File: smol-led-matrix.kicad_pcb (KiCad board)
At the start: 4 copper layers, 45.8 x 20.4 mm, 323 parts, among them J1 USB_C_Receptacle_USB2.0, J2 TagConnect_TC2030_SWD, Q1 FS8205, Q2 AO3401A, SW1 SW_Push, SW2 SW_Push, U1 STM32L433CBTx, U2 TP4054, U3 DW01+G, U4 XC6206P332MR

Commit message: Finish routing on first unit
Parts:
- added REF**: Perforation_0.2mm, Perforation:Perforation_0.2mm, F.Cu at (108.0, 142.7)
- added REF**: Perforation_0.2mm, Perforation:Perforation_0.2mm, F.Cu at (62.0, 131.8)
- added REF**: Perforation_0.2mm, Perforation:Perforation_0.2mm, F.Cu at (62.0, 129.8)
- added REF**: Perforation_0.2mm, Perforation:Perforation_0.2mm, F.Cu at (62.0, 138.7)
- added REF**: Perforation_0.2mm, Perforation:Perforation_0.2mm, F.Cu at (62.0, 140.7)
- added REF**: Perforation_0.2mm, Perforation:Perforation_0.2mm, F.Cu at (62.0, 142.7)
- added REF**: Perforation_0.2mm, Perforation:Perforation_0.2mm, F.Cu at (62.0, 139.7)
- added REF**: Perforation_0.2mm, Perforation:Perforation_0.2mm, F.Cu at (62.0, 141.2)
- added REF**: Perforation_0.2mm, Perforation:Perforation_0.2mm, F.Cu at (62.0, 139.2)
- added REF**: Perforation_0.2mm, Perforation:Perforation_0.2mm, F.Cu at (62.0, 141.7)
- added REF**: Perforation_0.2mm, Perforation:Perforation_0.2mm, F.Cu at (62.0, 138.2)
- added REF**: Perforation_0.2mm, Perforation:Perforation_0.2mm, F.Cu at (62.0, 128.3)
- added REF**: Perforation_0.2mm, Perforation:Perforation_0.2mm, F.Cu at (62.0, 142.2)
- added REF**: Perforation_0.2mm, Perforation:Perforation_0.2mm, F.Cu at (62.0, 140.2)
- added REF**: Perforation_0.2mm, Perforation:Perforation_0.2mm, F.Cu at (108.0, 139.3)
- added REF**: Perforation_0.2mm, Perforation:Perforation_0.2mm, F.Cu at (108.0, 141.2)
- added REF**: Perforation_0.2mm, Perforation:Perforation_0.2mm, F.Cu at (108.0, 142.2)
- added REF**: Perforation_0.2mm, Perforation:Perforation_0.2mm, F.Cu at (108.0, 140.8)
- added REF**: Perforation_0.2mm, Perforation:Perforation_0.2mm, F.Cu at (108.0, 140.2)
- added REF**: Perforation_0.2mm, Perforation:Perforation_0.2mm, F.Cu at (108.0, 139.8)
- added REF**: Perforation_0.2mm, Perforation:Perforation_0.2mm, F.Cu at (108.0, 138.8)
- added REF**: Perforation_0.2mm, Perforation:Perforation_0.2mm, F.Cu at (108.0, 138.2)
- added REF**: Perforation_0.2mm, Perforation:Perforation_0.2mm, F.Cu at (62.0, 130.3)
- added REF**: Perforation_0.2mm, Perforation:Perforation_0.2mm, F.Cu at (108.0, 141.8)
- added REF**: Perforation_0.2mm, Perforation:Perforation_0.2mm, F.Cu at (108.0, 132.3)
- added REF**: Perforation_0.2mm, Perforation:Perforation_0.2mm, F.Cu at (108.0, 130.3)
- added REF**: Perforation_0.2mm, Perforation:Perforation_0.2mm, F.Cu at (108.0, 128.8)
- added REF**: Perforation_0.2mm, Perforation:Perforation_0.2mm, F.Cu at (108.0, 127.8)
- added REF**: Perforation_0.2mm, Perforation:Perforation_0.2mm, F.Cu at (108.0, 131.8)
- added REF**: Perforation_0.2mm, Perforation:Perforation_0.2mm, F.Cu at (108.0, 128.3)
- added REF**: Perforation_0.2mm, Perforation:Perforation_0.2mm, F.Cu at (108.0, 130.8)
- added REF**: Perforation_0.2mm, Perforation:Perforation_0.2mm, F.Cu at (108.0, 131.3)
- added REF**: Perforation_0.2mm, Perforation:Perforation_0.2mm, F.Cu at (108.0, 129.3)
- added REF**: Perforation_0.2mm, Perforation:Perforation_0.2mm, F.Cu at (62.0, 132.3)
- added REF**: Perforation_0.2mm, Perforation:Perforation_0.2mm, F.Cu at (108.0, 129.8)
- added REF**: Perforation_0.2mm, Perforation:Perforation_0.2mm, F.Cu at (82.6, 140.2)
- added REF**: Perforation_0.2mm, Perforation:Perforation_0.2mm, F.Cu at (82.6, 140.8)
- added REF**: Perforation_0.2mm, Perforation:Perforation_0.2mm, F.Cu at (82.6, 142.8)
- added REF**: Perforation_0.2mm, Perforation:Perforation_0.2mm, F.Cu at (82.6, 143.7)
- added REF**: Perforation_0.2mm, Perforation:Perforation_0.2mm, F.Cu at (82.6, 144.2)
- added REF**: Perforation_0.2mm, Perforation:Perforation_0.2mm, F.Cu at (82.6, 143.2)
- added REF**: Perforation_0.2mm, Perforation:Perforation_0.2mm, F.Cu at (82.6, 144.8)
- added REF**: Perforation_0.2mm, Perforation:Perforation_0.2mm, F.Cu at (82.6, 141.2)
- added REF**: Perforation_0.2mm, Perforation:Perforation_0.2mm, F.Cu at (82.6, 141.8)
- added REF**: Perforation_0.2mm, Perforation:Perforation_0.2mm, F.Cu at (62.0, 129.3)
- added REF**: Perforation_0.2mm, Perforation:Perforation_0.2mm, F.Cu at (82.6, 142.2)
- added REF**: Perforation_0.2mm, Perforation:Perforation_0.2mm, F.Cu at (87.4, 144.8)
- added REF**: Perforation_0.2mm, Perforation:Perforation_0.2mm, F.Cu at (87.4, 144.2)
- added REF**: Perforation_0.2mm, Perforation:Perforation_0.2mm, F.Cu at (87.4, 142.2)
- added REF**: Perforation_0.2mm, Perforation:Perforation_0.2mm, F.Cu at (87.4, 141.3)
- added REF**: Perforation_0.2mm, Perforation:Perforation_0.2mm, F.Cu at (87.4, 140.8)
- added REF**: Perforation_0.2mm, Perforation:Perforation_0.2mm, F.Cu at (87.4, 141.8)
- added REF**: Perforation_0.2mm, Perforation:Perforation_0.2mm, F.Cu at (87.4, 140.2)
- added REF**: Perforation_0.2mm, Perforation:Perforation_0.2mm, F.Cu at (87.4, 143.8)
- added REF**: Perforation_0.2mm, Perforation:Perforation_0.2mm, F.Cu at (87.4, 143.2)
- added REF**: Perforation_0.2mm, Perforation:Perforation_0.2mm, F.Cu at (62.0, 130.8)
- added REF**: Perforation_0.2mm, Perforation:Perforation_0.2mm, F.Cu at (87.4, 142.8)
- added REF**: Perforation_0.2mm, Perforation:Perforation_0.2mm, F.Cu at (82.6, 129.3)
- added REF**: Perforation_0.2mm, Perforation:Perforation_0.2mm, F.Cu at (82.6, 128.8)
- added REF**: Perforation_0.2mm, Perforation:Perforation_0.2mm, F.Cu at (82.6, 126.8)
- added REF**: Perforation_0.2mm, Perforation:Perforation_0.2mm, F.Cu at (82.6, 125.9)
- added REF**: Perforation_0.2mm, Perforation:Perforation_0.2mm, F.Cu at (82.6, 125.3)
- added REF**: Perforation_0.2mm, Perforation:Perforation_0.2mm, F.Cu at (82.6, 126.3)
- added REF**: Perforation_0.2mm, Perforation:Perforation_0.2mm, F.Cu at (82.6, 124.8)
- added REF**: Perforation_0.2mm, Perforation:Perforation_0.2mm, F.Cu at (82.6, 128.4)
- added REF**: Perforation_0.2mm, Perforation:Perforation_0.2mm, F.Cu at (82.6, 127.8)
- added REF**: Perforation_0.2mm, Perforation:Perforation_0.2mm, F.Cu at (62.0, 128.9)
- added REF**: Perforation_0.2mm, Perforation:Perforation_0.2mm, F.Cu at (82.6, 127.3)
- added REF**: Perforation_0.2mm, Perforation:Perforation_0.2mm, F.Cu at (87.3, 129.3)
- added REF**: Perforation_0.2mm, Perforation:Perforation_0.2mm, F.Cu at (87.3, 128.8)
- added REF**: Perforation_0.2mm, Perforation:Perforation_0.2mm, F.Cu at (87.3, 128.3)
- added REF**: Perforation_0.2mm, Perforation:Perforation_0.2mm, F.Cu at (87.3, 127.8)
- added REF**: Perforation_0.2mm, Perforation:Perforation_0.2mm, F.Cu at (87.3, 127.3)
- added REF**: Perforation_0.2mm, Perforation:Perforation_0.2mm, F.Cu at (87.3, 126.8)
- added REF**: Perforation_0.2mm, Perforation:Perforation_0.2mm, F.Cu at (87.3, 126.3)
- added REF**: Perforation_0.2mm, Perforation:Perforation_0.2mm, F.Cu at (87.3, 125.8)
- added REF**: Perforation_0.2mm, Perforation:Perforation_0.2mm, F.Cu at (87.3, 125.3)
- added REF**: Perforation_0.2mm, Perforation:Perforation_0.2mm, F.Cu at (62.0, 131.4)
- added REF**: Perforation_0.2mm, Perforation:Perforation_0.2mm, F.Cu at (87.3, 124.8)
- added REF**: Perforation_0.2mm, Perforation:Perforation_0.2mm, F.Cu at (62.0, 127.8)
- moved C1 46.2 mm to (94.8, 144.5)
- moved C4 46.2 mm to (107.0, 128.3)
- moved C8 46.2 mm to (89.2, 135.0)
- moved D106 46.2 mm to (72.3, 125.7)
- moved D107 46.2 mm to (72.3, 127.0)
- moved D110 46.2 mm to (72.3, 130.9)
- moved D112 46.2 mm to (72.3, 133.5)
- moved D113 46.2 mm to (72.3, 134.8)
- moved D115 46.2 mm to (72.3, 137.4)
- moved D117 46.2 mm to (72.3, 140.0)
- moved D118 46.2 mm to (72.3, 141.3)
- moved D120 46.2 mm to (72.3, 143.9)
- moved D121 46.2 mm to (73.6, 125.7)
- moved D122 46.2 mm to (73.6, 127.0)
- moved D123 46.2 mm to (73.6, 128.3)
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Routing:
- net /A0: track 45.3 -> 144.3 mm
- net /K1: track 35.9 -> 133.7 mm
- net /A7: track 26.2 -> 123.2 mm
- net /A8: track 26.6 -> 123.3 mm
- net /A6: track 26.3 -> 120.0 mm
- net /A9: track 26.1 -> 119.7 mm
- net /A5: track 26.6 -> 117.3 mm
- net /A10: track 26.3 -> 116.6 mm
- net /A14: track 37.0 -> 126.4 mm
- net /A4: track 26.9 -> 115.4 mm
- net /A11: track 28.3 -> 116.1 mm
- net /A3: track 36.0 -> 122.6 mm
- net /A12: track 32.6 -> 118.9 mm
- net /A2: track 38.0 -> 123.9 mm
- net /A1: track 41.3 -> 127.2 mm
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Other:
- board size 45.8 x 20.4 mm -> 61.8 x 100 mm

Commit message: Full panel
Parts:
- added C1: 100nF, Capacitor_SMD:C_0402_1005Metric, F.Cu at (94.8, 86.5)
- added C1: 100nF, Capacitor_SMD:C_0402_1005Metric, F.Cu at (94.8, 115.5)
- added C10: 10uF, Capacitor_SMD:C_0402_1005Metric, F.Cu at (99.9, 82.8)
- added C10: 10uF, Capacitor_SMD:C_0402_1005Metric, F.Cu at (99.9, 111.8)
- added C11: 100nF, Capacitor_SMD:C_0402_1005Metric, F.Cu at (88.2, 76.7)
- added C11: 100nF, Capacitor_SMD:C_0402_1005Metric, F.Cu at (88.2, 105.7)
- added C2: 100nF, Capacitor_SMD:C_0402_1005Metric, F.Cu at (88.0, 83.4)
- added C2: 100nF, Capacitor_SMD:C_0402_1005Metric, F.Cu at (88.0, 112.4)
- added C3: 1uF, Capacitor_SMD:C_0402_1005Metric, F.Cu at (100.5, 70.7)
- added C3: 1uF, Capacitor_SMD:C_0402_1005Metric, F.Cu at (100.5, 99.7)
- added C4: 100nF, Capacitor_SMD:C_0402_1005Metric, F.Cu at (107.0, 70.3)
- added C4: 100nF, Capacitor_SMD:C_0402_1005Metric, F.Cu at (107.0, 99.3)
- added C5: 100nF, Capacitor_SMD:C_0402_1005Metric, F.Cu at (93.0, 86.5)
- added C5: 100nF, Capacitor_SMD:C_0402_1005Metric, F.Cu at (93.0, 115.5)
- added C6: 1uF, Capacitor_SMD:C_0402_1005Metric, F.Cu at (101.9, 78.9)
- added C6: 1uF, Capacitor_SMD:C_0402_1005Metric, F.Cu at (101.9, 107.9)
- added C7: 1uF, Capacitor_SMD:C_0402_1005Metric, F.Cu at (103.6, 78.9)
- added C7: 1uF, Capacitor_SMD:C_0402_1005Metric, F.Cu at (103.6, 107.9)
- added C8: 100nF, Capacitor_SMD:C_0402_1005Metric, F.Cu at (89.2, 77.0)
- added C8: 100nF, Capacitor_SMD:C_0402_1005Metric, F.Cu at (89.2, 106.0)
- added C9: 100nF, Capacitor_SMD:C_0402_1005Metric, F.Cu at (97.5, 77.0)
- added C9: 100nF, Capacitor_SMD:C_0402_1005Metric, F.Cu at (97.5, 106.0)
- added D1: LED, LED_SMD:LED_0402_1005Metric, F.Cu at (63.2, 67.7)
- added D1: LED, LED_SMD:LED_0402_1005Metric, F.Cu at (63.2, 96.7)
- added D10: LED, LED_SMD:LED_0402_1005Metric, F.Cu at (63.2, 79.4)
- added D10: LED, LED_SMD:LED_0402_1005Metric, F.Cu at (63.2, 108.4)
- added D100: LED, LED_SMD:LED_0402_1005Metric, F.Cu at (71.0, 79.4)
- added D100: LED, LED_SMD:LED_0402_1005Metric, F.Cu at (71.0, 108.4)
- added D101: LED, LED_SMD:LED_0402_1005Metric, F.Cu at (71.0, 80.7)
- added D101: LED, LED_SMD:LED_0402_1005Metric, F.Cu at (71.0, 109.7)
- added D102: LED, LED_SMD:LED_0402_1005Metric, F.Cu at (71.0, 82.0)
- added D102: LED, LED_SMD:LED_0402_1005Metric, F.Cu at (71.0, 111.0)
- added D103: LED, LED_SMD:LED_0402_1005Metric, F.Cu at (71.0, 83.3)
- added D103: LED, LED_SMD:LED_0402_1005Metric, F.Cu at (71.0, 112.3)
- added D104: LED, LED_SMD:LED_0402_1005Metric, F.Cu at (71.0, 84.6)
- added D104: LED, LED_SMD:LED_0402_1005Metric, F.Cu at (71.0, 113.6)
- added D105: LED, LED_SMD:LED_0402_1005Metric, F.Cu at (71.0, 85.9)
- added D105: LED, LED_SMD:LED_0402_1005Metric, F.Cu at (71.0, 114.9)
- added D106: LED, LED_SMD:LED_0402_1005Metric, F.Cu at (72.3, 67.7)
- added D106: LED, LED_SMD:LED_0402_1005Metric, F.Cu at (72.3, 96.7)
- added D107: LED, LED_SMD:LED_0402_1005Metric, F.Cu at (72.3, 69.0)
- added D107: LED, LED_SMD:LED_0402_1005Metric, F.Cu at (72.3, 98.0)
- added D108: LED, LED_SMD:LED_0402_1005Metric, F.Cu at (72.3, 70.3)
- added D108: LED, LED_SMD:LED_0402_1005Metric, F.Cu at (72.3, 99.3)
- added D109: LED, LED_SMD:LED_0402_1005Metric, F.Cu at (72.3, 71.6)
- added D109: LED, LED_SMD:LED_0402_1005Metric, F.Cu at (72.3, 100.6)
- added D11: LED, LED_SMD:LED_0402_1005Metric, F.Cu at (63.2, 80.7)
- added D11: LED, LED_SMD:LED_0402_1005Metric, F.Cu at (63.2, 109.7)
- added D110: LED, LED_SMD:LED_0402_1005Metric, F.Cu at (72.3, 72.9)
- added D110: LED, LED_SMD:LED_0402_1005Metric, F.Cu at (72.3, 101.9)
- added D111: LED, LED_SMD:LED_0402_1005Metric, F.Cu at (72.3, 74.2)
- added D111: LED, LED_SMD:LED_0402_1005Metric, F.Cu at (72.3, 103.2)
- added D112: LED, LED_SMD:LED_0402_1005Metric, F.Cu at (72.3, 75.5)
- added D112: LED, LED_SMD:LED_0402_1005Metric, F.Cu at (72.3, 104.5)
- added D113: LED, LED_SMD:LED_0402_1005Metric, F.Cu at (72.3, 76.8)
- added D113: LED, LED_SMD:LED_0402_1005Metric, F.Cu at (72.3, 105.8)
- added D114: LED, LED_SMD:LED_0402_1005Metric, F.Cu at (72.3, 78.1)
- added D114: LED, LED_SMD:LED_0402_1005Metric, F.Cu at (72.3, 107.1)
- added D115: LED, LED_SMD:LED_0402_1005Metric, F.Cu at (72.3, 79.4)
- added D115: LED, LED_SMD:LED_0402_1005Metric, F.Cu at (72.3, 108.4)
- added D116: LED, LED_SMD:LED_0402_1005Metric, F.Cu at (72.3, 80.7)
- added D116: LED, LED_SMD:LED_0402_1005Metric, F.Cu at (72.3, 109.7)
- added D117: LED, LED_SMD:LED_0402_1005Metric, F.Cu at (72.3, 82.0)
- added D117: LED, LED_SMD:LED_0402_1005Metric, F.Cu at (72.3, 111.0)
- added D118: LED, LED_SMD:LED_0402_1005Metric, F.Cu at (72.3, 83.3)
- added D118: LED, LED_SMD:LED_0402_1005Metric, F.Cu at (72.3, 112.3)
- added D119: LED, LED_SMD:LED_0402_1005Metric, F.Cu at (72.3, 84.6)
- added D119: LED, LED_SMD:LED_0402_1005Metric, F.Cu at (72.3, 113.6)
- added D12: LED, LED_SMD:LED_0402_1005Metric, F.Cu at (63.2, 82.0)
- added D12: LED, LED_SMD:LED_0402_1005Metric, F.Cu at (63.2, 111.0)
- added D120: LED, LED_SMD:LED_0402_1005Metric, F.Cu at (72.3, 85.9)
- added D120: LED, LED_SMD:LED_0402_1005Metric, F.Cu at (72.3, 114.9)
- added D121: LED, LED_SMD:LED_0402_1005Metric, F.Cu at (73.6, 67.7)
- added D121: LED, LED_SMD:LED_0402_1005Metric, F.Cu at (73.6, 96.7)
- added D122: LED, LED_SMD:LED_0402_1005Metric, F.Cu at (73.6, 69.0)
- added D122: LED, LED_SMD:LED_0402_1005Metric, F.Cu at (73.6, 98.0)
- added D123: LED, LED_SMD:LED_0402_1005Metric, F.Cu at (73.6, 70.3)
- added D123: LED, LED_SMD:LED_0402_1005Metric, F.Cu at (73.6, 99.3)
- added D124: LED, LED_SMD:LED_0402_1005Metric, F.Cu at (73.6, 71.6)
- added D124: LED, LED_SMD:LED_0402_1005Metric, F.Cu at (73.6, 100.6)
- added D125: LED, LED_SMD:LED_0402_1005Metric, F.Cu at (73.6, 72.9)
- added D125: LED, LED_SMD:LED_0402_1005Metric, F.Cu at (73.6, 101.9)
- added D126: LED, LED_SMD:LED_0402_1005Metric, F.Cu at (73.6, 74.2)
- added D126: LED, LED_SMD:LED_0402_1005Metric, F.Cu at (73.6, 103.2)
- added D127: LED, LED_SMD:LED_0402_1005Metric, F.Cu at (73.6, 75.5)
- added D127: LED, LED_SMD:LED_0402_1005Metric, F.Cu at (73.6, 104.5)
- added D128: LED, LED_SMD:LED_0402_1005Metric, F.Cu at (73.6, 76.8)
- added D128: LED, LED_SMD:LED_0402_1005Metric, F.Cu at (73.6, 105.8)
- added D129: LED, LED_SMD:LED_0402_1005Metric, F.Cu at (73.6, 78.1)
- added D129: LED, LED_SMD:LED_0402_1005Metric, F.Cu at (73.6, 107.1)
- added D13: LED, LED_SMD:LED_0402_1005Metric, F.Cu at (63.2, 83.3)
- added D13: LED, LED_SMD:LED_0402_1005Metric, F.Cu at (63.2, 112.3)
- added D130: LED, LED_SMD:LED_0402_1005Metric, F.Cu at (73.6, 79.4)
- added D130: LED, LED_SMD:LED_0402_1005Metric, F.Cu at (73.6, 108.4)
- added D131: LED, LED_SMD:LED_0402_1005Metric, F.Cu at (73.6, 80.7)
- added D131: LED, LED_SMD:LED_0402_1005Metric, F.Cu at (73.6, 109.7)
- added D132: LED, LED_SMD:LED_0402_1005Metric, F.Cu at (73.6, 82.0)
- added D132: LED, LED_SMD:LED_0402_1005Metric, F.Cu at (73.6, 111.0)
- added D133: LED, LED_SMD:LED_0402_1005Metric, F.Cu at (73.6, 83.3)
- added D133: LED, LED_SMD:LED_0402_1005Metric, F.Cu at (73.6, 112.3)
- added D134: LED, LED_SMD:LED_0402_1005Metric, F.Cu at (73.6, 84.6)
- added D134: LED, LED_SMD:LED_0402_1005Metric, F.Cu at (73.6, 113.6)
- added D135: LED, LED_SMD:LED_0402_1005Metric, F.Cu at (73.6, 85.9)
- added D135: LED, LED_SMD:LED_0402_1005Metric, F.Cu at (73.6, 114.9)
- added D136: LED, LED_SMD:LED_0402_1005Metric, F.Cu at (74.9, 67.7)
- added D136: LED, LED_SMD:LED_0402_1005Metric, F.Cu at (74.9, 96.7)
- added D137: LED, LED_SMD:LED_0402_1005Metric, F.Cu at (74.9, 69.0)
- added D137: LED, LED_SMD:LED_0402_1005Metric, F.Cu at (74.9, 98.0)
- added D138: LED, LED_SMD:LED_0402_1005Metric, F.Cu at (74.9, 70.3)
- added D138: LED, LED_SMD:LED_0402_1005Metric, F.Cu at (74.9, 99.3)
- added D139: LED, LED_SMD:LED_0402_1005Metric, F.Cu at (74.9, 71.6)
- added D139: LED, LED_SMD:LED_0402_1005Metric, F.Cu at (74.9, 100.6)
- added D14: LED, LED_SMD:LED_0402_1005Metric, F.Cu at (63.2, 84.6)
- added D14: LED, LED_SMD:LED_0402_1005Metric, F.Cu at (63.2, 113.6)
- added D140: LED, LED_SMD:LED_0402_1005Metric, F.Cu at (74.9, 72.9)
- added D140: LED, LED_SMD:LED_0402_1005Metric, F.Cu at (74.9, 101.9)
- added D141: LED, LED_SMD:LED_0402_1005Metric, F.Cu at (74.9, 74.2)
- added D141: LED, LED_SMD:LED_0402_1005Metric, F.Cu at (74.9, 103.2)
- added D142: LED, LED_SMD:LED_0402_1005Metric, F.Cu at (74.9, 75.5)
- added D142: LED, LED_SMD:LED_0402_1005Metric, F.Cu at (74.9, 104.5)
- added D143: LED, LED_SMD:LED_0402_1005Metric, F.Cu at (74.9, 76.8)
- added D143: LED, LED_SMD:LED_0402_1005Metric, F.Cu at (74.9, 105.8)
- added D144: LED, LED_SMD:LED_0402_1005Metric, F.Cu at (74.9, 78.1)
- added D144: LED, LED_SMD:LED_0402_1005Metric, F.Cu at (74.9, 107.1)
- added D145: LED, LED_SMD:LED_0402_1005Metric, F.Cu at (74.9, 79.4)
- added D145: LED, LED_SMD:LED_0402_1005Metric, F.Cu at (74.9, 108.4)
- added D146: LED, LED_SMD:LED_0402_1005Metric, F.Cu at (74.9, 80.7)
- added D146: LED, LED_SMD:LED_0402_1005Metric, F.Cu at (74.9, 109.7)
- added D147: LED, LED_SMD:LED_0402_1005Metric, F.Cu at (74.9, 82.0)
- added D147: LED, LED_SMD:LED_0402_1005Metric, F.Cu at (74.9, 111.0)
- added D148: LED, LED_SMD:LED_0402_1005Metric, F.Cu at (74.9, 83.3)
- added D148: LED, LED_SMD:LED_0402_1005Metric, F.Cu at (74.9, 112.3)
- added D149: LED, LED_SMD:LED_0402_1005Metric, F.Cu at (74.9, 84.6)
- added D149: LED, LED_SMD:LED_0402_1005Metric, F.Cu at (74.9, 113.6)
- added D15: LED, LED_SMD:LED_0402_1005Metric, F.Cu at (63.2, 85.9)
- added D15: LED, LED_SMD:LED_0402_1005Metric, F.Cu at (63.2, 114.9)
- added D150: LED, LED_SMD:LED_0402_1005Metric, F.Cu at (74.9, 85.9)
- added D150: LED, LED_SMD:LED_0402_1005Metric, F.Cu at (74.9, 114.9)
- added D151: LED, LED_SMD:LED_0402_1005Metric, F.Cu at (76.2, 67.7)
- added D151: LED, LED_SMD:LED_0402_1005Metric, F.Cu at (76.2, 96.7)
- added D152: LED, LED_SMD:LED_0402_1005Metric, F.Cu at (76.2, 69.0)
- added D152: LED, LED_SMD:LED_0402_1005Metric, F.Cu at (76.2, 98.0)
- added D153: LED, LED_SMD:LED_0402_1005Metric, F.Cu at (76.2, 70.3)
- added D153: LED, LED_SMD:LED_0402_1005Metric, F.Cu at (76.2, 99.3)
- added D154: LED, LED_SMD:LED_0402_1005Metric, F.Cu at (76.2, 71.6)
- added D154: LED, LED_SMD:LED_0402_1005Metric, F.Cu at (76.2, 100.6)
- added D155: LED, LED_SMD:LED_0402_1005Metric, F.Cu at (76.2, 72.9)
- added D155: LED, LED_SMD:LED_0402_1005Metric, F.Cu at (76.2, 101.9)
- added D156: LED, LED_SMD:LED_0402_1005Metric, F.Cu at (76.2, 74.2)
- added D156: LED, LED_SMD:LED_0402_1005Metric, F.Cu at (76.2, 103.2)
- added D157: LED, LED_SMD:LED_0402_1005Metric, F.Cu at (76.2, 75.5)
- added D157: LED, LED_SMD:LED_0402_1005Metric, F.Cu at (76.2, 104.5)
- added D158: LED, LED_SMD:LED_0402_1005Metric, F.Cu at (76.2, 76.8)
- added D158: LED, LED_SMD:LED_0402_1005Metric, F.Cu at (76.2, 105.8)
- added D159: LED, LED_SMD:LED_0402_1005Metric, F.Cu at (76.2, 78.1)
- added D159: LED, LED_SMD:LED_0402_1005Metric, F.Cu at (76.2, 107.1)
- added D16: LED, LED_SMD:LED_0402_1005Metric, F.Cu at (64.5, 67.7)
- added D16: LED, LED_SMD:LED_0402_1005Metric, F.Cu at (64.5, 96.7)
- added D160: LED, LED_SMD:LED_0402_1005Metric, F.Cu at (76.2, 79.4)
- added D160: LED, LED_SMD:LED_0402_1005Metric, F.Cu at (76.2, 108.4)
- added D161: LED, LED_SMD:LED_0402_1005Metric, F.Cu at (76.2, 80.7)
- added D161: LED, LED_SMD:LED_0402_1005Metric, F.Cu at (76.2, 109.7)
- added D162: LED, LED_SMD:LED_0402_1005Metric, F.Cu at (76.2, 82.0)
- added D162: LED, LED_SMD:LED_0402_1005Metric, F.Cu at (76.2, 111.0)
- added D163: LED, LED_SMD:LED_0402_1005Metric, F.Cu at (76.2, 83.3)
- added D163: LED, LED_SMD:LED_0402_1005Metric, F.Cu at (76.2, 112.3)
- added D164: LED, LED_SMD:LED_0402_1005Metric, F.Cu at (76.2, 84.6)
- added D164: LED, LED_SMD:LED_0402_1005Metric, F.Cu at (76.2, 113.6)
- added D165: LED, LED_SMD:LED_0402_1005Metric, F.Cu at (76.2, 85.9)
- added D165: LED, LED_SMD:LED_0402_1005Metric, F.Cu at (76.2, 114.9)
- added D166: LED, LED_SMD:LED_0402_1005Metric, F.Cu at (77.5, 67.7)
- added D166: LED, LED_SMD:LED_0402_1005Metric, F.Cu at (77.5, 96.7)
- added D167: LED, LED_SMD:LED_0402_1005Metric, F.Cu at (77.5, 69.0)
- added D167: LED, LED_SMD:LED_0402_1005Metric, F.Cu at (77.5, 98.0)
- added D168: LED, LED_SMD:LED_0402_1005Metric, F.Cu at (77.5, 70.3)
- added D168: LED, LED_SMD:LED_0402_1005Metric, F.Cu at (77.5, 99.3)
- added D169: LED, LED_SMD:LED_0402_1005Metric, F.Cu at (77.5, 71.6)
- added D169: LED, LED_SMD:LED_0402_1005Metric, F.Cu at (77.5, 100.6)
- added D17: LED, LED_SMD:LED_0402_1005Metric, F.Cu at (64.5, 69.0)
- added D17: LED, LED_SMD:LED_0402_1005Metric, F.Cu at (64.5, 98.0)
- added D170: LED, LED_SMD:LED_0402_1005Metric, F.Cu at (77.5, 72.9)
- added D170: LED, LED_SMD:LED_0402_1005Metric, F.Cu at (77.5, 101.9)
- added D171: LED, LED_SMD:LED_0402_1005Metric, F.Cu at (77.5, 74.2)
- added D171: LED, LED_SMD:LED_0402_1005Metric, F.Cu at (77.5, 103.2)
- added D172: LED, LED_SMD:LED_0402_1005Metric, F.Cu at (77.5, 75.5)
- added D172: LED, LED_SMD:LED_0402_1005Metric, F.Cu at (77.5, 104.5)
- added D173: LED, LED_SMD:LED_0402_1005Metric, F.Cu at (77.5, 76.8)
- added D173: LED, LED_SMD:LED_0402_1005Metric, F.Cu at (77.5, 105.8)
- added D174: LED, LED_SMD:LED_0402_1005Metric, F.Cu at (77.5, 78.1)
- added D174: LED, LED_SMD:LED_0402_1005Metric, F.Cu at (77.5, 107.1)
- added D175: LED, LED_SMD:LED_0402_1005Metric, F.Cu at (77.5, 79.4)
- added D175: LED, LED_SMD:LED_0402_1005Metric, F.Cu at (77.5, 108.4)
- added D176: LED, LED_SMD:LED_0402_1005Metric, F.Cu at (77.5, 80.7)
- added D176: LED, LED_SMD:LED_0402_1005Metric, F.Cu at (77.5, 109.7)
- added D177: LED, LED_SMD:LED_0402_1005Metric, F.Cu at (77.5, 82.0)
- added D177: LED, LED_SMD:LED_0402_1005Metric, F.Cu at (77.5, 111.0)
- added D178: LED, LED_SMD:LED_0402_1005Metric, F.Cu at (77.5, 83.3)
- added D178: LED, LED_SMD:LED_0402_1005Metric, F.Cu at (77.5, 112.3)
- added D179: LED, LED_SMD:LED_0402_1005Metric, F.Cu at (77.5, 84.6)
- added D179: LED, LED_SMD:LED_0402_1005Metric, F.Cu at (77.5, 113.6)
- added D18: LED, LED_SMD:LED_0402_1005Metric, F.Cu at (64.5, 70.3)
- added D18: LED, LED_SMD:LED_0402_1005Metric, F.Cu at (64.5, 99.3)
- added D180: LED, LED_SMD:LED_0402_1005Metric, F.Cu at (77.5, 85.9)
- added D180: LED, LED_SMD:LED_0402_1005Metric, F.Cu at (77.5, 114.9)
- added D181: LED, LED_SMD:LED_0402_1005Metric, F.Cu at (78.8, 67.7)
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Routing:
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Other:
- board size 61.8 x 100 mm -> 61.8 x 88.2 mm
- board text added: "JLCJLCJLCJLC"
- board text added: "SMØL MATRIX RevA Designed by Tobias Schramm 2020"

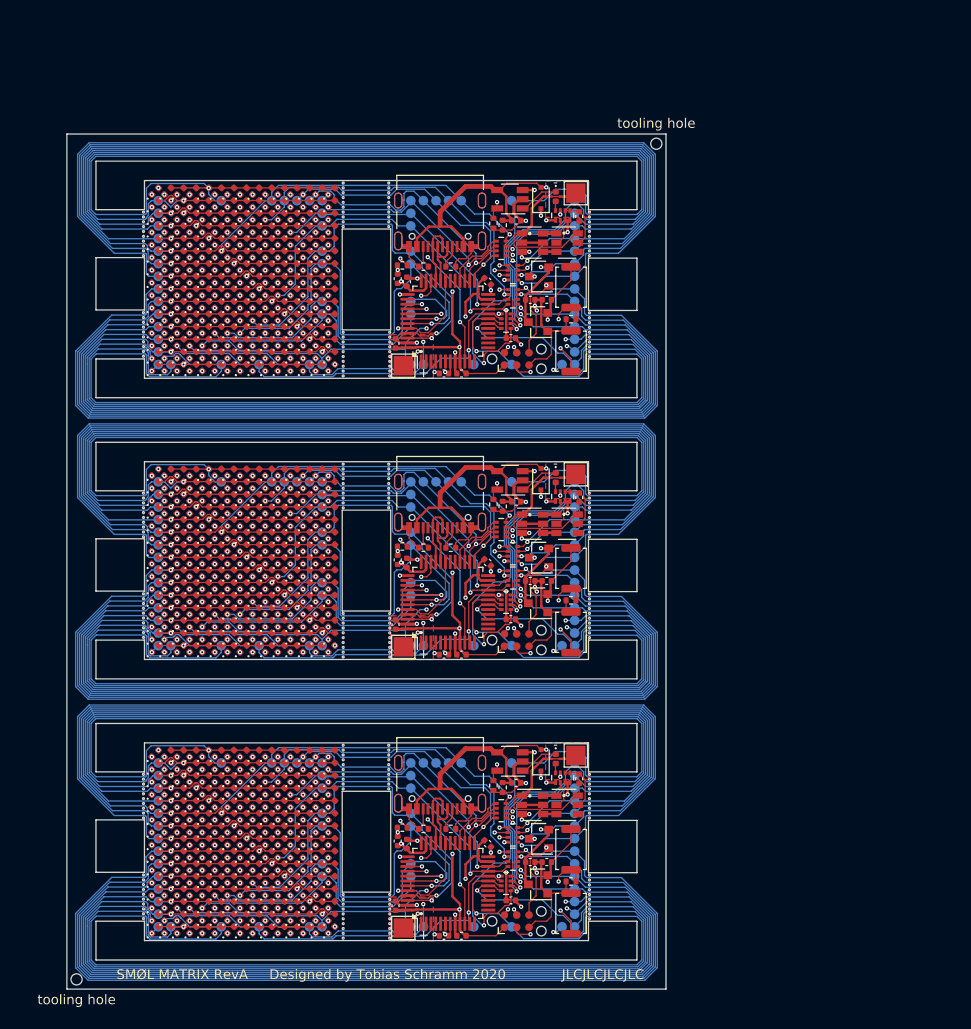
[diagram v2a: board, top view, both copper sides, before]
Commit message: Fix clearances for JLC board manufacturing
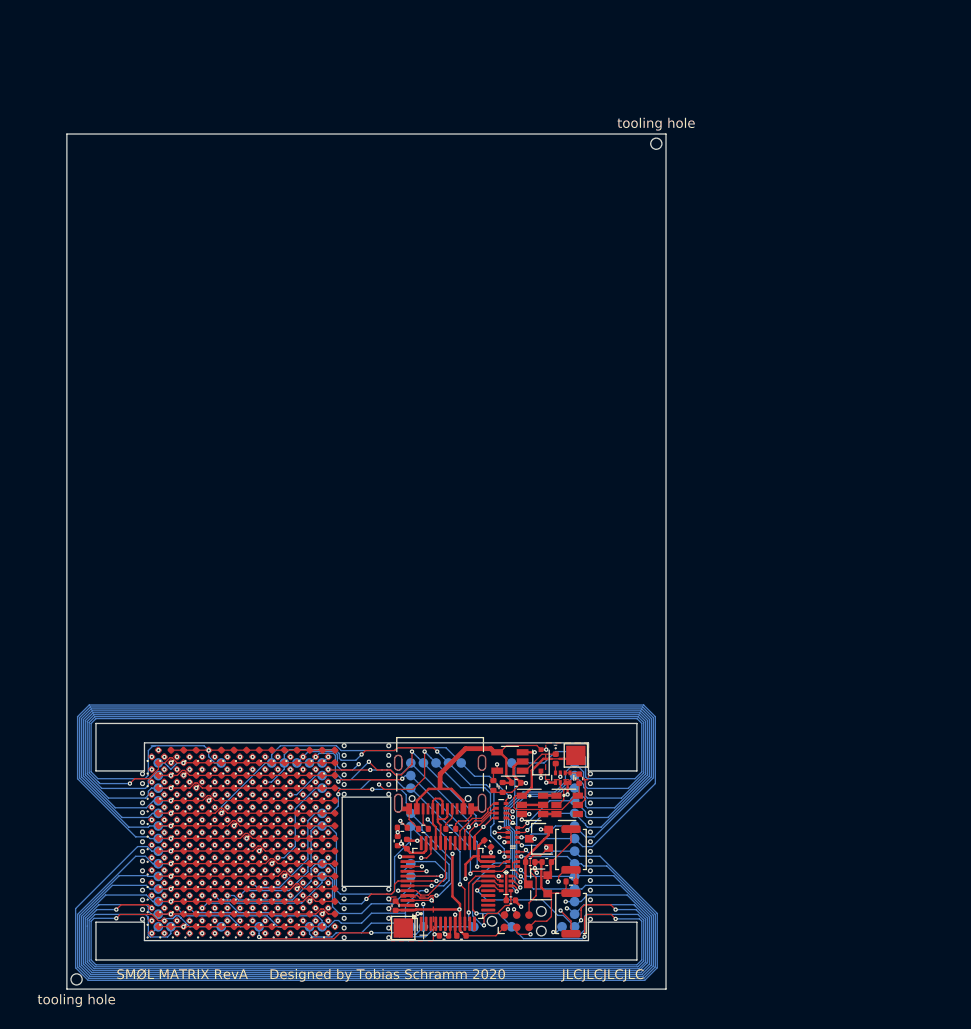
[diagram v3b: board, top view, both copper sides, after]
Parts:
- removed the C1 at (94.8, 86.5)
- removed the C1 at (94.8, 115.5)
- removed the C10 at (99.9, 82.8)
- removed the C10 at (99.9, 111.8)
- removed the C11 at (88.2, 76.7)
- removed the C11 at (88.2, 105.7)
- removed the C2 at (88.0, 83.4)
- removed the C2 at (88.0, 112.4)
- removed the C3 at (100.5, 70.7)
- removed the C3 at (100.5, 99.7)
- removed the C4 at (107.0, 70.3)
- removed the C4 at (107.0, 99.3)
- removed the C5 at (93.0, 86.5)
- removed the C5 at (93.0, 115.5)
- removed the C6 at (101.9, 78.9)
- removed the C6 at (101.9, 107.9)
- removed the C7 at (103.6, 78.9)
- removed the C7 at (103.6, 107.9)
- removed the C8 at (89.2, 77.0)
- removed the C8 at (89.2, 106.0)
- removed the C9 at (97.5, 77.0)
- removed the C9 at (97.5, 106.0)
- removed the D1 at (63.2, 67.7)
- removed the D1 at (63.2, 96.7)
- removed the D10 at (63.2, 79.4)
- removed the D10 at (63.2, 108.4)
- removed the D100 at (71.0, 79.4)
- removed the D100 at (71.0, 108.4)
- removed the D101 at (71.0, 80.7)
- removed the D101 at (71.0, 109.7)
- removed the D102 at (71.0, 82.0)
- removed the D102 at (71.0, 111.0)
- removed the D103 at (71.0, 83.3)
- removed the D103 at (71.0, 112.3)
- removed the D104 at (71.0, 84.6)
- removed the D104 at (71.0, 113.6)
- removed the D105 at (71.0, 85.9)
- removed the D105 at (71.0, 114.9)
- removed the D106 at (72.3, 67.7)
- removed the D106 at (72.3, 96.7)
- removed the D107 at (72.3, 69.0)
- removed the D107 at (72.3, 98.0)
- removed the D108 at (72.3, 70.3)
- removed the D108 at (72.3, 99.3)
- removed the D109 at (72.3, 71.6)
- removed the D109 at (72.3, 100.6)
- removed the D11 at (63.2, 80.7)
- removed the D11 at (63.2, 109.7)
- removed the D110 at (72.3, 72.9)
- removed the D110 at (72.3, 101.9)
- removed the D111 at (72.3, 74.2)
- removed the D111 at (72.3, 103.2)
- removed the D112 at (72.3, 75.5)
- removed the D112 at (72.3, 104.5)
- removed the D113 at (72.3, 76.8)
- removed the D113 at (72.3, 105.8)
- removed the D114 at (72.3, 78.1)
- removed the D114 at (72.3, 107.1)
- removed the D115 at (72.3, 79.4)
- removed the D115 at (72.3, 108.4)
- removed the D116 at (72.3, 80.7)
- removed the D116 at (72.3, 109.7)
- removed the D117 at (72.3, 82.0)
- removed the D117 at (72.3, 111.0)
- removed the D118 at (72.3, 83.3)
- removed the D118 at (72.3, 112.3)
- removed the D119 at (72.3, 84.6)
- removed the D119 at (72.3, 113.6)
- removed the D12 at (63.2, 82.0)
- removed the D12 at (63.2, 111.0)
- removed the D120 at (72.3, 85.9)
- removed the D120 at (72.3, 114.9)
- removed the D121 at (73.6, 67.7)
- removed the D121 at (73.6, 96.7)
- removed the D122 at (73.6, 69.0)
- removed the D122 at (73.6, 98.0)
- removed the D123 at (73.6, 70.3)
- removed the D123 at (73.6, 99.3)
- removed the D124 at (73.6, 71.6)
- removed the D124 at (73.6, 100.6)
- removed the D125 at (73.6, 72.9)
- removed the D125 at (73.6, 101.9)
- removed the D126 at (73.6, 74.2)
- removed the D126 at (73.6, 103.2)
- removed the D127 at (73.6, 75.5)
- removed the D127 at (73.6, 104.5)
- removed the D128 at (73.6, 76.8)
- removed the D128 at (73.6, 105.8)
- removed the D129 at (73.6, 78.1)
- removed the D129 at (73.6, 107.1)
- removed the D13 at (63.2, 83.3)
- removed the D13 at (63.2, 112.3)
- removed the D130 at (73.6, 79.4)
- removed the D130 at (73.6, 108.4)
- removed the D131 at (73.6, 80.7)
- removed the D131 at (73.6, 109.7)
- removed the D132 at (73.6, 82.0)
- removed the D132 at (73.6, 111.0)
- removed the D133 at (73.6, 83.3)
- removed the D133 at (73.6, 112.3)
- removed the D134 at (73.6, 84.6)
- removed the D134 at (73.6, 113.6)
- removed the D135 at (73.6, 85.9)
- removed the D135 at (73.6, 114.9)
- removed the D136 at (74.9, 67.7)
- removed the D136 at (74.9, 96.7)
- removed the D137 at (74.9, 69.0)
- removed the D137 at (74.9, 98.0)
- removed the D138 at (74.9, 70.3)
- removed the D138 at (74.9, 99.3)
- removed the D139 at (74.9, 71.6)
- removed the D139 at (74.9, 100.6)
- removed the D14 at (63.2, 84.6)
- removed the D14 at (63.2, 113.6)
- removed the D140 at (74.9, 72.9)
- removed the D140 at (74.9, 101.9)
- removed the D141 at (74.9, 74.2)
- removed the D141 at (74.9, 103.2)
- removed the D142 at (74.9, 75.5)
- removed the D142 at (74.9, 104.5)
- removed the D143 at (74.9, 76.8)
- removed the D143 at (74.9, 105.8)
- removed the D144 at (74.9, 78.1)
- removed the D144 at (74.9, 107.1)
- removed the D145 at (74.9, 79.4)
- removed the D145 at (74.9, 108.4)
- removed the D146 at (74.9, 80.7)
- removed the D146 at (74.9, 109.7)
- removed the D147 at (74.9, 82.0)
- removed the D147 at (74.9, 111.0)
- removed the D148 at (74.9, 83.3)
- removed the D148 at (74.9, 112.3)
- removed the D149 at (74.9, 84.6)
- removed the D149 at (74.9, 113.6)
- removed the D15 at (63.2, 85.9)
- removed the D15 at (63.2, 114.9)
- removed the D150 at (74.9, 85.9)
- removed the D150 at (74.9, 114.9)
- removed the D151 at (76.2, 67.7)
- removed the D151 at (76.2, 96.7)
- removed the D152 at (76.2, 69.0)
- removed the D152 at (76.2, 98.0)
- removed the D153 at (76.2, 70.3)
- removed the D153 at (76.2, 99.3)
- removed the D154 at (76.2, 71.6)
- removed the D154 at (76.2, 100.6)
- removed the D155 at (76.2, 72.9)
- removed the D155 at (76.2, 101.9)
- removed the D156 at (76.2, 74.2)
- removed the D156 at (76.2, 103.2)
- removed the D157 at (76.2, 75.5)
- removed the D157 at (76.2, 104.5)
- removed the D158 at (76.2, 76.8)
- removed the D158 at (76.2, 105.8)
- removed the D159 at (76.2, 78.1)
- removed the D159 at (76.2, 107.1)
- removed the D16 at (64.5, 67.7)
- removed the D16 at (64.5, 96.7)
- removed the D160 at (76.2, 79.4)
- removed the D160 at (76.2, 108.4)
- removed the D161 at (76.2, 80.7)
- removed the D161 at (76.2, 109.7)
- removed the D162 at (76.2, 82.0)
- removed the D162 at (76.2, 111.0)
- removed the D163 at (76.2, 83.3)
- removed the D163 at (76.2, 112.3)
- removed the D164 at (76.2, 84.6)
- removed the D164 at (76.2, 113.6)
- removed the D165 at (76.2, 85.9)
- removed the D165 at (76.2, 114.9)
- removed the D166 at (77.5, 67.7)
- removed the D166 at (77.5, 96.7)
- removed the D167 at (77.5, 69.0)
- removed the D167 at (77.5, 98.0)
- removed the D168 at (77.5, 70.3)
- removed the D168 at (77.5, 99.3)
- removed the D169 at (77.5, 71.6)
- removed the D169 at (77.5, 100.6)
- removed the D17 at (64.5, 69.0)
- removed the D17 at (64.5, 98.0)
- removed the D170 at (77.5, 72.9)
- removed the D170 at (77.5, 101.9)
- removed the D171 at (77.5, 74.2)
- removed the D171 at (77.5, 103.2)
- removed the D172 at (77.5, 75.5)
- removed the D172 at (77.5, 104.5)
- removed the D173 at (77.5, 76.8)
- removed the D173 at (77.5, 105.8)
- removed the D174 at (77.5, 78.1)
- removed the D174 at (77.5, 107.1)
- removed the D175 at (77.5, 79.4)
- removed the D175 at (77.5, 108.4)
- removed the D176 at (77.5, 80.7)
- removed the D176 at (77.5, 109.7)
- removed the D177 at (77.5, 82.0)
- removed the D177 at (77.5, 111.0)
- removed the D178 at (77.5, 83.3)
- removed the D178 at (77.5, 112.3)
- removed the D179 at (77.5, 84.6)
- removed the D179 at (77.5, 113.6)
- removed the D18 at (64.5, 70.3)
- removed the D18 at (64.5, 99.3)
- removed the D180 at (77.5, 85.9)
- removed the D180 at (77.5, 114.9)
- removed the D181 at (78.8, 67.7)
- removed the D181 at (78.8, 96.7)
- removed the D182 at (78.8, 69.0)
- removed the D182 at (78.8, 98.0)
- removed the D183 at (78.8, 70.3)
- removed the D183 at (78.8, 99.3)
- removed the D184 at (78.8, 71.6)
- removed the D184 at (78.8, 100.6)
- removed the D185 at (78.8, 72.9)
- removed the D185 at (78.8, 101.9)
- removed the D186 at (78.8, 74.2)
- removed the D186 at (78.8, 103.2)
- removed the D187 at (78.8, 75.5)
- removed the D187 at (78.8, 104.5)
- removed the D188 at (78.8, 76.8)
- removed the D188 at (78.8, 105.8)
- removed the D189 at (78.8, 78.1)
- removed the D189 at (78.8, 107.1)
- removed the D19 at (64.5, 71.6)
- removed the D19 at (64.5, 100.6)
- removed the D190 at (78.8, 79.4)
- removed the D190 at (78.8, 108.4)
- removed the D191 at (78.8, 80.7)
- removed the D191 at (78.8, 109.7)
- removed the D192 at (78.8, 82.0)
- removed the D192 at (78.8, 111.0)
- removed the D193 at (78.8, 83.3)
- removed the D193 at (78.8, 112.3)
- removed the D194 at (78.8, 84.6)
- removed the D194 at (78.8, 113.6)
- removed the D195 at (78.8, 85.9)
- removed the D195 at (78.8, 114.9)
- removed the D196 at (80.1, 67.7)
- removed the D196 at (80.1, 96.7)
- removed the D197 at (80.1, 69.0)
- removed the D197 at (80.1, 98.0)
- removed the D198 at (80.1, 70.3)
- removed the D198 at (80.1, 99.3)
- removed the D199 at (80.1, 71.6)
- removed the D199 at (80.1, 100.6)
- removed the D2 at (63.2, 69.0)
- removed the D2 at (63.2, 98.0)
- removed the D20 at (64.5, 72.9)
- removed the D20 at (64.5, 101.9)
- removed the D200 at (80.1, 72.9)
- removed the D200 at (80.1, 101.9)
- removed the D201 at (80.1, 74.2)
- removed the D201 at (80.1, 103.2)
- removed the D202 at (80.1, 75.5)
- removed the D202 at (80.1, 104.5)
- removed the D203 at (80.1, 76.8)
- removed the D203 at (80.1, 105.8)
- removed the D204 at (80.1, 78.1)
- removed the D204 at (80.1, 107.1)
- removed the D205 at (80.1, 79.4)
- removed the D205 at (80.1, 108.4)
- removed the D206 at (80.1, 80.7)
- removed the D206 at (80.1, 109.7)
- removed the D207 at (80.1, 82.0)
- removed the D207 at (80.1, 111.0)
- removed the D208 at (80.1, 83.3)
- removed the D208 at (80.1, 112.3)
- removed the D209 at (80.1, 84.6)
- removed the D209 at (80.1, 113.6)
- removed the D21 at (64.5, 74.2)
- removed the D21 at (64.5, 103.2)
- removed the D210 at (80.1, 85.9)
- removed the D210 at (80.1, 114.9)
- removed the D211 at (81.4, 67.7)
- removed the D211 at (81.4, 96.7)
- removed the D212 at (81.4, 69.0)
- removed the D212 at (81.4, 98.0)
- removed the D213 at (81.4, 70.3)
- removed the D213 at (81.4, 99.3)
- removed the D214 at (81.4, 71.6)
- removed the D214 at (81.4, 100.6)
- removed the D215 at (81.4, 72.9)
- removed the D215 at (81.4, 101.9)
- removed the D216 at (81.4, 74.2)
- removed the D216 at (81.4, 103.2)
- removed the D217 at (81.4, 75.5)
- removed the D217 at (81.4, 104.5)
- removed the D218 at (81.4, 76.8)
- removed the D218 at (81.4, 105.8)
- removed the D219 at (81.4, 78.1)
- removed the D219 at (81.4, 107.1)
- removed the D22 at (64.5, 75.5)
- removed the D22 at (64.5, 104.5)
- removed the D220 at (81.4, 79.4)
- removed the D220 at (81.4, 108.4)
- removed the D221 at (81.4, 80.7)
- removed the D221 at (81.4, 109.7)
- removed the D222 at (81.4, 82.0)
- removed the D222 at (81.4, 111.0)
- removed the D223 at (81.4, 83.3)
- removed the D223 at (81.4, 112.3)
- removed the D224 at (81.4, 84.6)
- removed the D224 at (81.4, 113.6)
- removed the D225 at (81.4, 85.9)
- removed the D225 at (81.4, 114.9)
- removed the D226 at (104.5, 68.2)
- removed the D226 at (104.5, 97.2)
- removed the D227 at (103.0, 68.4)
- removed the D227 at (103.0, 97.4)
- removed the D23 at (64.5, 76.8)
- removed the D23 at (64.5, 105.8)
- removed the D24 at (64.5, 78.1)
- removed the D24 at (64.5, 107.1)
- removed the D25 at (64.5, 79.4)
- removed the D25 at (64.5, 108.4)
- removed the D26 at (64.5, 80.7)
- removed the D26 at (64.5, 109.7)
- removed the D27 at (64.5, 82.0)
- removed the D27 at (64.5, 111.0)
- removed the D28 at (64.5, 83.3)
- removed the D28 at (64.5, 112.3)
- removed the D29 at (64.5, 84.6)
- removed the D29 at (64.5, 113.6)
- removed the D3 at (63.2, 70.3)
- removed the D3 at (63.2, 99.3)
- removed the D30 at (64.5, 85.9)
- removed the D30 at (64.5, 114.9)
- removed the D31 at (65.8, 67.7)
- removed the D31 at (65.8, 96.7)
- removed the D32 at (65.8, 69.0)
- removed the D32 at (65.8, 98.0)
- removed the D33 at (65.8, 70.3)
- removed the D33 at (65.8, 99.3)
- removed the D34 at (65.8, 71.6)
- removed the D34 at (65.8, 100.6)
- removed the D35 at (65.8, 72.9)
- removed the D35 at (65.8, 101.9)
- removed the D36 at (65.8, 74.2)
- removed the D36 at (65.8, 103.2)
- removed the D37 at (65.8, 75.5)
- removed the D37 at (65.8, 104.5)
- removed the D38 at (65.8, 76.8)
- removed the D38 at (65.8, 105.8)
- removed the D39 at (65.8, 78.1)
- removed the D39 at (65.8, 107.1)
- removed the D4 at (63.2, 71.6)
- removed the D4 at (63.2, 100.6)
- removed the D40 at (65.8, 79.4)
- removed the D40 at (65.8, 108.4)
- removed the D41 at (65.8, 80.7)
- removed the D41 at (65.8, 109.7)
- removed the D42 at (65.8, 82.0)
- removed the D42 at (65.8, 111.0)
- removed the D43 at (65.8, 83.3)
- removed the D43 at (65.8, 112.3)
- removed the D44 at (65.8, 84.6)
- removed the D44 at (65.8, 113.6)
- removed the D45 at (65.8, 85.9)
- removed the D45 at (65.8, 114.9)
- removed the D46 at (67.1, 67.7)
- removed the D46 at (67.1, 96.7)
- removed the D47 at (67.1, 69.0)
- removed the D47 at (67.1, 98.0)
- removed the D48 at (67.1, 70.3)
- removed the D48 at (67.1, 99.3)
- removed the D49 at (67.1, 71.6)
- removed the D49 at (67.1, 100.6)
- removed the D5 at (63.2, 72.9)
- removed the D5 at (63.2, 101.9)
- removed the D50 at (67.1, 72.9)
- removed the D50 at (67.1, 101.9)
- removed the D51 at (67.1, 74.2)
- removed the D51 at (67.1, 103.2)
- removed the D52 at (67.1, 75.5)
- removed the D52 at (67.1, 104.5)
- removed the D53 at (67.1, 76.8)
- removed the D53 at (67.1, 105.8)
- removed the D54 at (67.1, 78.1)
- removed the D54 at (67.1, 107.1)
- removed the D55 at (67.1, 79.4)
- removed the D55 at (67.1, 108.4)
- removed the D56 at (67.1, 80.7)
- removed the D56 at (67.1, 109.7)
- removed the D57 at (67.1, 82.0)
- removed the D57 at (67.1, 111.0)
- removed the D58 at (67.1, 83.3)
- removed the D58 at (67.1, 112.3)
- removed the D59 at (67.1, 84.6)
- removed the D59 at (67.1, 113.6)
- removed the D6 at (63.2, 74.2)
- removed the D6 at (63.2, 103.2)
- removed the D60 at (67.1, 85.9)
- removed the D60 at (67.1, 114.9)
- removed the D61 at (68.4, 67.7)
- removed the D61 at (68.4, 96.7)
- removed the D62 at (68.4, 69.0)
- removed the D62 at (68.4, 98.0)
- removed the D63 at (68.4, 70.3)
- removed the D63 at (68.4, 99.3)
- removed the D64 at (68.4, 71.6)
- removed the D64 at (68.4, 100.6)
- removed the D65 at (68.4, 72.9)
- removed the D65 at (68.4, 101.9)
- removed the D66 at (68.4, 74.2)
- removed the D66 at (68.4, 103.2)
- removed the D67 at (68.4, 75.5)
- removed the D67 at (68.4, 104.5)
- removed the D68 at (68.4, 76.8)
- removed the D68 at (68.4, 105.8)
- removed the D69 at (68.4, 78.1)
- removed the D69 at (68.4, 107.1)
- removed the D7 at (63.2, 75.5)
- removed the D7 at (63.2, 104.5)
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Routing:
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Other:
- outline, holes or cut-outs redrawn
